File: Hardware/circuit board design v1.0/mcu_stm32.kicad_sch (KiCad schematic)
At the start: 13 parts, among them U1 STM32F446RETx, U2 W25Q64JVSS, U3 SDR08540M3-01

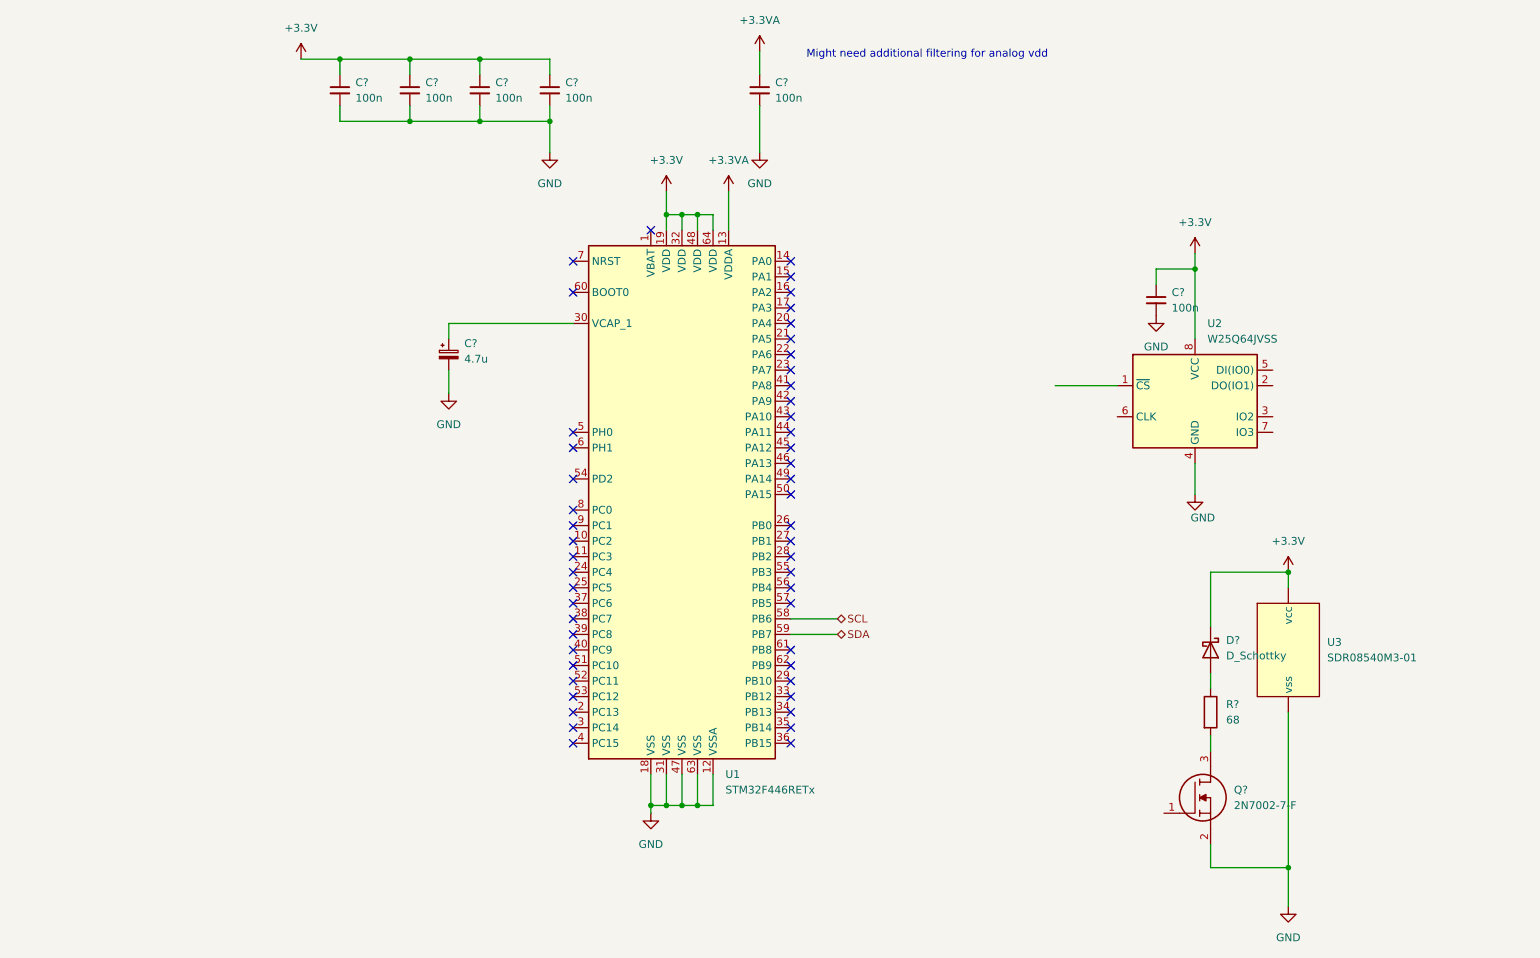
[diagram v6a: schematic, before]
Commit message: Created stm32mx project and started on layout
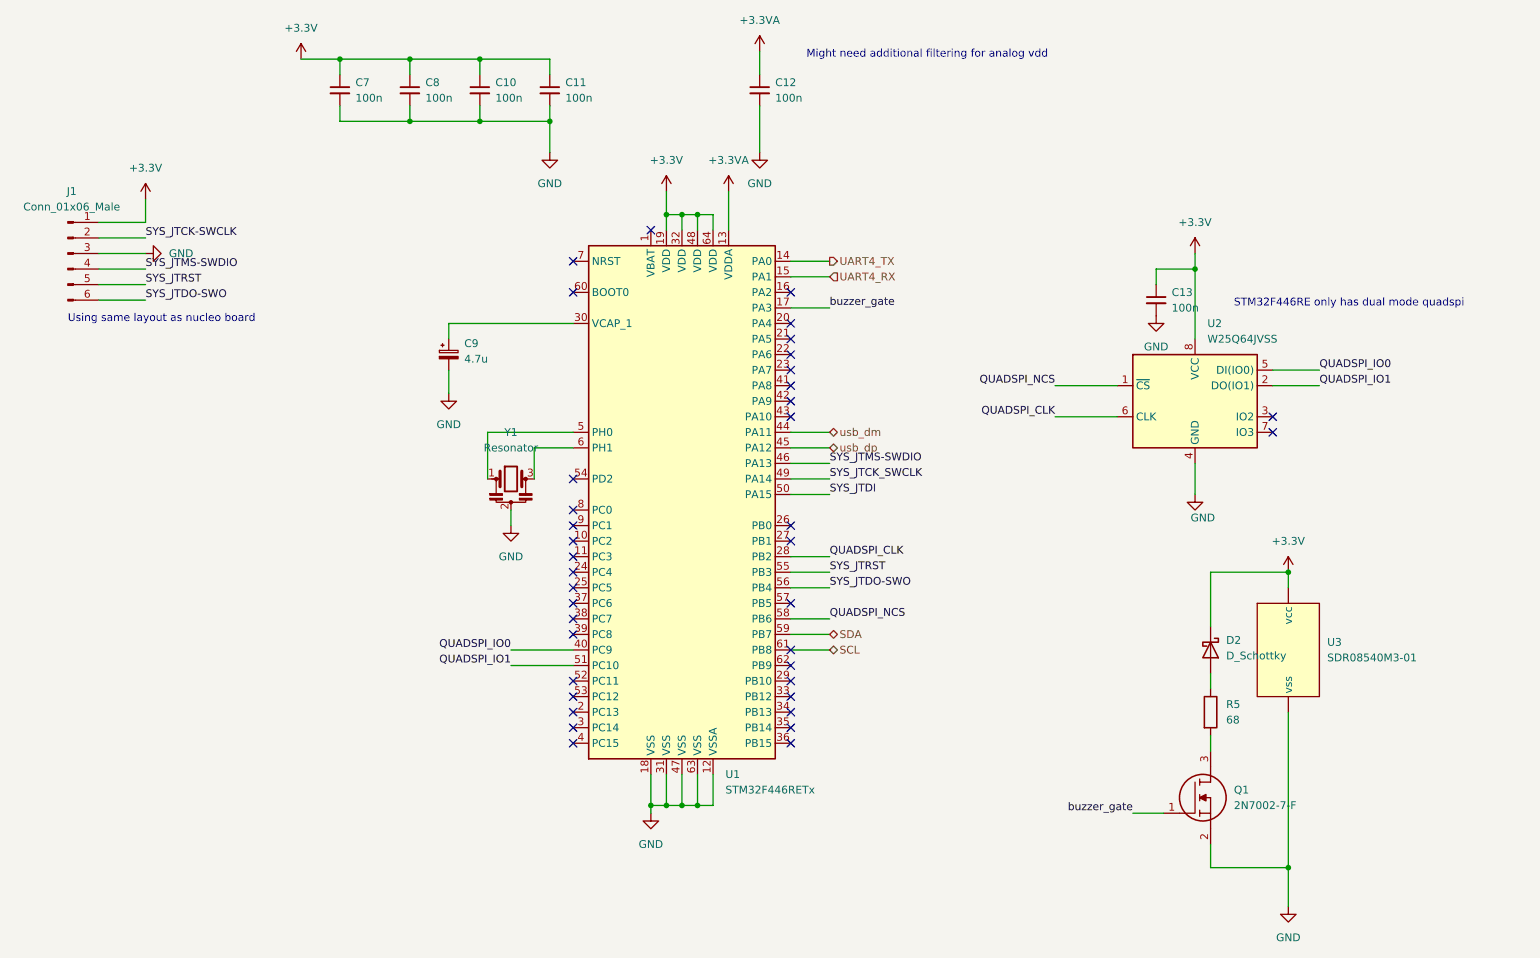
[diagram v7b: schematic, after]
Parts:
- added J1: Conn_01x06_Male, Connector_PinHeader_2.54mm:PinHeader_1x06_P2.54mm_Vertical, symbol Connector:Conn_01x06_Male
- added Y1: Resonator, symbol Device:Resonator
- D2: renamed from D?; footprint (none) -> Components:PowerDI123
- R5: renamed from R?; footprint Resistor_SMD:R_0603_1608Metric_Pad0.98x0.95mm_HandSolder -> Resistor_SMD:R_0603_1608Metric
- gave numbers to parts that had none: 8
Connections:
- net +3.3V: now also J1.1 (Pin_1)
- net GND: now also J1.3 (Pin_3), Y1.2
- net SCL: now also U1.61 (PB8); no longer U1.58 (PB6)
- net QUADSPI_NCS: now reaches U2.1 (~{CS})
- net QUADSPI_NCS: now also U1.58 (PB6)
- net QUADSPI_IO1: now reaches U2.2 (DO(IO1))
- net QUADSPI_IO1: now also U1.51 (PC10)
- net QUADSPI_IO0: now reaches U2.5 (DI(IO0))
- net QUADSPI_IO0: now also U1.40 (PC9)
- net QUADSPI_CLK: now reaches U2.6 (CLK)
- net QUADSPI_CLK: now also U1.28 (PB2)
- net buzzer_gate: now reaches Q1.1
- net buzzer_gate: now also U1.17 (PA3)
- net UART4_TX: now reaches U1.14 (PA0)
- net UART4_RX: now reaches U1.15 (PA1)
- net usb_dm: now reaches U1.44 (PA11)
- net usb_dp: now reaches U1.45 (PA12)
- net SYS_JTMS-SWDIO: now reaches U1.46 (PA13)
- net SYS_JTMS-SWDIO: now also J1.4 (Pin_4)
- net SYS_JTCK_SWCLK: now reaches U1.49 (PA14)
- net at U1.5 (PH0): now also Y1.1
- net SYS_JTDI: now reaches U1.50 (PA15)
- net SYS_JTRST: now reaches U1.55 (PB3)
- net SYS_JTRST: now also J1.5 (Pin_5)
- net SYS_JTDO-SWO: now reaches U1.56 (PB4)
- net SYS_JTDO-SWO: now also J1.6 (Pin_6)
- net at U1.6 (PH1): now also Y1.3
- new net SYS_JTCK-SWCLK: J1.2 (Pin_2)
- no-connect marks 51 -> 38
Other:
- note added: "STM32F446RE only has dual mode quadspi"
- note added: "Using same layout as nucleo board"

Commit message: Added spi connection for radio
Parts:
- added J4: Conn_01x04, symbol Connector_Generic:Conn_01x04
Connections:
- net SPI1_SCK: now reaches U1.21 (PA5)
- net SPI1_SCK: now also J4.4 (Pin_4)
- net SPI1_MISO: now reaches U1.22 (PA6)
- net SPI1_MISO: now also J4.3 (Pin_3)
- net SPI1_MOSI: now reaches U1.23 (PA7)
- net SPI1_MOSI: now also J4.2 (Pin_2)
- net Radio_Enable: now reaches U1.24 (PC4)
- net Radio_Enable: now also J4.1 (Pin_1)
- no-connect marks 38 -> 34
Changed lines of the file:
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@@
   )
   (no_connect (at 144.78 49.53))
-  (no_connect (at 167.64 69.85))
-  (no_connect (at 167.64 72.39))
   (no_connect (at 167.64 74.93))
   (no_connect (at 167.64 77.47))
@@
   (no_connect (at 167.64 59.69))
   (no_connect (at 167.64 64.77))
-  (no_connect (at 167.64 67.31))
   (no_connect (at 167.64 110.49))
   (no_connect (at 167.64 118.11))
@@
   (no_connect (at 132.08 100.33))
   (no_connect (at 132.08 102.87))
-  (no_connect (at 132.08 105.41))
   (no_connect (at 132.08 90.17))
   (no_connect (at 132.08 107.95))
@@
     (stroke (width 0) (type default) (color 0 0 0 0))
   )
+  (wire (pts (xy 167.64 69.85) (xy 173.99 69.85))
+    (stroke (width 0) (type default) (color 0 0 0 0))
+  )
   (wire (pts (xy 105.41 21.59) (xy 105.41 24.13))
     (stroke (width 0) (type default) (color 0 0 0 0))
@@
     (stroke (width 0) (type default) (color 0 0 0 0))
   )
+  (wire (pts (xy 167.64 72.39) (xy 173.99 72.39))
+    (stroke (width 0) (type default) (color 0 0 0 0))
+  )
   (wire (pts (xy 167.64 102.87) (xy 173.99 102.87))
     (stroke (width 0) (type default) (color 0 0 0 0))
   )
+  (wire (pts (xy 57.15 81.28) (xy 62.23 81.28))
+    (stroke (width 0) (type default) (color 0 0 0 0))
+  )
   (wire (pts (xy 162.56 20.32) (xy 162.56 24.13))
     (stroke (width 0) (type default) (color 0 0 0 0))
   )
+  (wire (pts (xy 121.92 105.41) (xy 132.08 105.41))
+    (stroke (width 0) (type default) (color 0 0 0 0))
+  )
   (wire (pts (xy 111.76 64.77) (xy 132.08 64.77))
     (stroke (width 0) (type default) (color 0 0 0 0))
@@
     (stroke (width 0) (type default) (color 0 0 0 0))
   )
+  (wire (pts (xy 57.15 78.74) (xy 62.23 78.74))
+    (stroke (width 0) (type default) (color 0 0 0 0))
+  )
   (wire (pts (xy 87.63 21.59) (xy 93.98 21.59))
     (stroke (width 0) (type default) (color 0 0 0 0))
@@
     (stroke (width 0) (type default) (color 0 0 0 0))
   )
+  (wire (pts (xy 57.15 76.2) (xy 62.23 76.2))
+    (stroke (width 0) (type default) (color 0 0 0 0))
+  )
   (wire (pts (xy 62.23 44.45) (xy 62.23 48.26))
     (stroke (width 0) (type default) (color 0 0 0 0))
@@
     (stroke (width 0) (type default) (color 0 0 0 0))
   )
+  (wire (pts (xy 57.15 73.66) (xy 62.23 73.66))
+    (stroke (width 0) (type default) (color 0 0 0 0))
+  )
   (wire (pts (xy 233.68 53.34) (xy 233.68 55.88))
     (stroke (width 0) (type default) (color 0 0 0 0))
@@
     (stroke (width 0) (type default) (color 0 0 0 0))
   )
+  (wire (pts (xy 167.64 67.31) (xy 173.99 67.31))
+    (stroke (width 0) (type default) (color 0 0 0 0))
+  )
   (wire (pts (xy 167.64 90.17) (xy 173.99 90.17))
     (stroke (width 0) (type default) (color 0 0 0 0))
@@
   )
   (text "Might need additional filtering for analog vdd\n" (at 170.18 21.59 0)
+    (effects (font (size 1.27 1.27)) (justify left bottom))
+  )
+  (label "SPI1_MISO" (at 62.23 76.2 0)
     (effects (font (size 1.27 1.27)) (justify left bottom))
   )
@@
     (effects (font (size 1.27 1.27)) (justify right bottom))
   )
+  (label "Radio_Enable" (at 62.23 81.28 0)
+    (effects (font (size 1.27 1.27)) (justify left bottom))
+  )
+  (label "SPI1_SCK" (at 173.99 67.31 0)
+    (effects (font (size 1.27 1.27)) (justify left bottom))
+  )
+  (label "Radio_Enable" (at 121.92 105.41 180)
+    (effects (font (size 1.27 1.27)) (justify right bottom))
+  )
+  (label "SPI1_MISO" (at 173.99 69.85 0)
+    (effects (font (size 1.27 1.27)) (justify left bottom))
+  )
   (label "SYS_JTDI" (at 173.99 92.71 0)
     (effects (font (size 1.27 1.27)) (justify left bottom))
@@
     (effects (font (size 1.27 1.27)) (justify left bottom))
   )
+  (label "SPI1_MOSI" (at 173.99 72.39 0)
+    (effects (font (size 1.27 1.27)) (justify left bottom))
+  )
   (label "QUADSPI_IO0" (at 254 72.39 0)
     (effects (font (size 1.27 1.27)) (justify left bottom))
@@
   )
   (label "QUADSPI_IO1" (at 254 74.93 0)
+    (effects (font (size 1.27 1.27)) (justify left bottom))
+  )
+  (label "SPI1_SCK" (at 62.23 73.66 0)
     (effects (font (size 1.27 1.27)) (justify left bottom))
   )
@@
   (label "QUADSPI_NCS" (at 210.82 74.93 180)
     (effects (font (size 1.27 1.27)) (justify right bottom))
+  )
+  (label "SPI1_MOSI" (at 62.23 78.74 0)
+    (effects (font (size 1.27 1.27)) (justify left bottom))
   )
   (label "SYS_JTDO-SWO" (at 173.99 107.95 0)
@@
     (pin "1")
   )
+  (symbol (lib_id "Connector_Generic:Conn_01x04") (at 52.07 78.74 180) (unit 1)
+    (in_bom yes) (on_board yes) (fields_autoplaced)
+    (property "Reference" "J4" (id 0) (at 52.07 67.31 0))
+    (property "Value" "Conn_01x04" (id 1) (at 52.07 69.85 0))
+    (property "Footprint" "" (id 2) (at 52.07 78.74 0)
+      (effects (font (size 1.27 1.27)) hide)
+    )
+    (property "Datasheet" "~" (id 3) (at 52.07 78.74 0)
+      (effects (font (size 1.27 1.27)) hide)
+    )
+    (pin "1")
+    (pin "2")
+    (pin "3")
+    (pin "4")
+  )
   (symbol (lib_id "power:+3.3V") (at 147.32 43.18 0) (unit 1)
